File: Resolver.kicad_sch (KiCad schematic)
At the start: 102 parts, among them Q10 BC807, Q11 BC817, Q12 BC807, Q4 BC817, Q5 BC817, Q6 BC817, Q7 BC807, Q8 BC807, Q9 BC817, U13 LMV321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

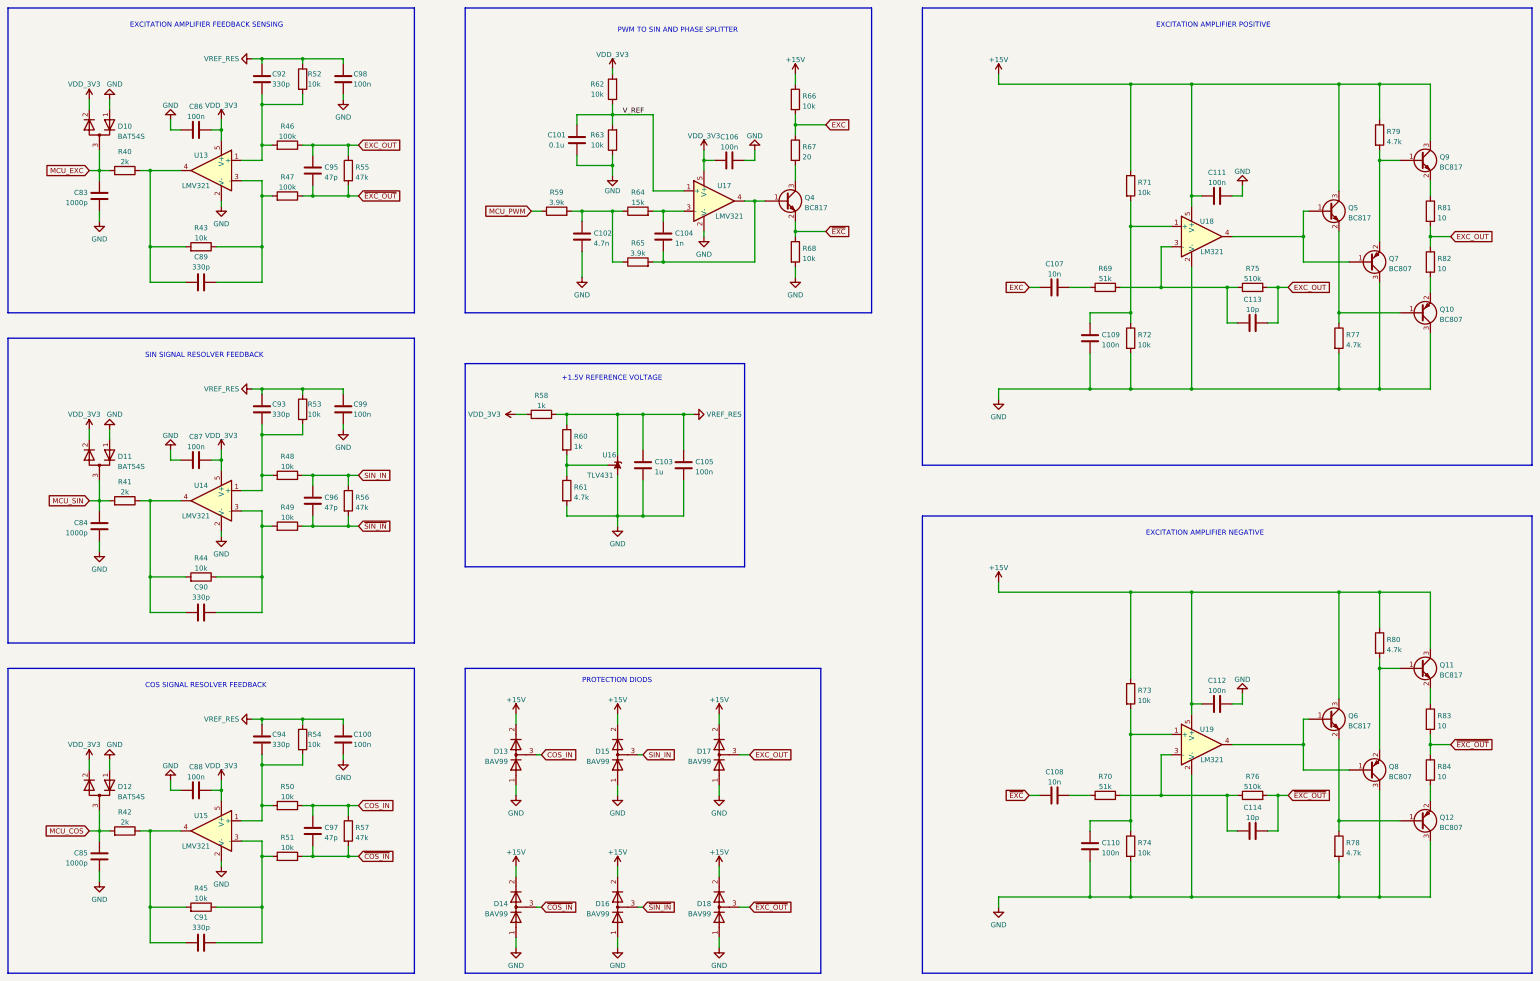
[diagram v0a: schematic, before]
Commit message: Изменения в схеме: убрал разъемы датчиков тока
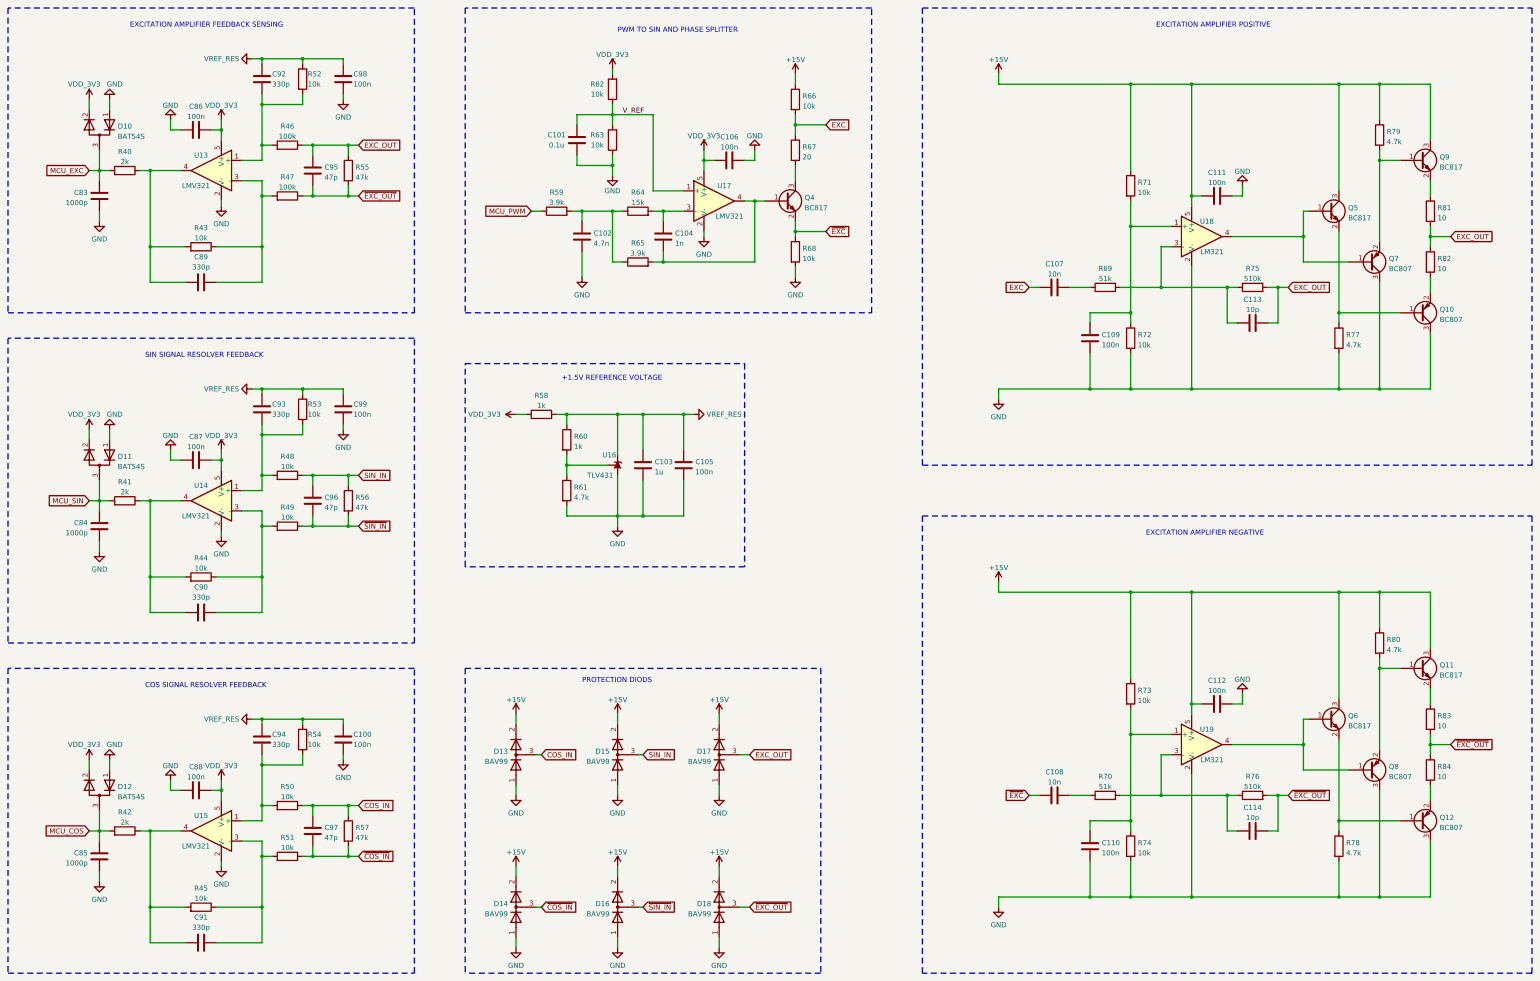
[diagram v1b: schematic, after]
